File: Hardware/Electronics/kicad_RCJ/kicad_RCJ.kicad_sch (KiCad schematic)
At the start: 66 parts, among them J1 Raspberry_Pi_2_3, J2 Conn_01x06, J3 Conn_01x02, J4 Conn_01x02, J5 Conn_01x02, J6 Conn_01x02, J7 Conn_01x01, U20 BNO085, U21 ICM20948, U22 LSM6DSOX+LIS3MDL, U23 TCS34725, U24 APDS9960

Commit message: schematic finished?
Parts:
- removed D1, D2: ~, symbol RCJ_parts:small_LED
- removed F1: Fuse, symbol Device:Fuse
- added J10, J11, J12, J13, J15: Conn_01x04, symbol Connector_Generic:Conn_01x04
- added J14: Conn_01x06_teensy_left, symbol Connector_Generic:Conn_01x06
- added J16: Conn_01x07, symbol Connector_Generic:Conn_01x07
- added J8: Conn_01x03, symbol Connector_Generic:Conn_01x03
- added J9: Conn_01x06_LED, symbol Connector_Generic:Conn_01x06
- added U25: ~, symbol RCJ_parts:VL53L0X/VL53L1X
- J4: value Conn_01x02 -> Conn_01x02_5V
- J5: value Conn_01x02 -> Conn_01x02_3V3
- J6: value Conn_01x02 -> Conn_01x02_I2C
- J7: value Conn_01x01 -> Conn_01x01_LOP
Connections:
- net +3.3V: now also U25.2 (VIN)
- net +5V: now also D3.2 (VIN), D4.2 (VIN), D5.2 (VIN), D6.2 (VIN), D7.1 (VIN), D8.1 (VIN); no longer J1.2 (5V)
- net GND: now also U6.44 (GND), U25.3 (GND); no longer J1.6 (GND)
- net SCL: now also U25.5 (SCL)
- net SCL1: no longer J1.5 (SCL/GPIO3)
- net SDA: now also U25.4 (SDA)
- net SDA1: no longer J1.3 (SDA/GPIO2)
- net at R14.1, U10.1 (VIN), U11.1 (VIN)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: now also BT1.1 (+)
- net at U19.1 (PA0): now also J16.7 (Pin_7)
- net at U19.16 (PB7): now also U25.6 (XSHUT)
- net at U19.19 (IB): now also J8.3 (Pin_3)
- net at U19.2 (PA1): now also J16.6 (Pin_6)
- net at U19.20 (RST): now also J8.2 (Pin_2)
- net at U19.21 (IA): now also J8.1 (Pin_1)
- net at U19.3 (PA2): now also J16.5 (Pin_5)
- net at U19.4 (PA3): now also J16.4 (Pin_4)
- net at U19.5 (PA4): now also J16.3 (Pin_3)
- net at U19.6 (PA5): now also J16.2 (Pin_2)
- net at U19.7 (PA6): now also J16.1 (Pin_1)
- net at D8.2 (SIGNAL): now also J9.1 (Pin_1); no longer D7.2 (SIGNAL)
- net at D5.3 (SIGNAL): now also J9.5 (Pin_5)
- net at U1.12 (IMODE): now also J10.1 (Pin_1)
- net at U1.13 (FAULT): now also J10.2 (Pin_2)
- net at U1.14 (CS): now also J10.3 (Pin_3)
- net at U1.7 (VREF): now also J10.4 (Pin_4)
- net at D3.3 (SIGNAL): now also J9.4 (Pin_4)
- net at D6.3 (SIGNAL): now also J9.6 (Pin_6)
- net at U2.12 (IMODE): now also J11.1 (Pin_1)
- net at U2.13 (FAULT): now also J11.2 (Pin_2)
- net at U2.14 (CS): now also J11.3 (Pin_3)
- net at U2.7 (VREF): now also J11.4 (Pin_4)
- net at U4.12 (IMODE): now also J13.1 (Pin_1)
- net at U4.13 (FAULT): now also J13.2 (Pin_2)
- net at U4.14 (CS): now also J13.3 (Pin_3)
- net at U4.7 (VREF): now also J13.4 (Pin_4)
- net at U3.12 (IMODE): now also J12.1 (Pin_1)
- net at U3.13 (FAULT): now also J12.2 (Pin_2)
- net at U3.14 (CS): now also J12.3 (Pin_3)
- net at U3.7 (VREF): now also J12.4 (Pin_4)
- net at D4.3 (SIGNAL): now also J9.3 (Pin_3)
- net at U6.12 (12/MISO): now also J14.6 (Pin_6)
- net at U6.21 (21/A7/RX5): now also J15.1 (Pin_1)
- net at U6.24 (24/A10/TX6/SCL2): now also J14.5 (Pin_5)
- net at U6.25 (25/A11/RX6/SDA2): now also J14.4 (Pin_4)
- net at U6.26 (26/A12/MOSI1): now also J14.3 (Pin_3)
- net at U6.27 (27/A13/SCK1): now also J14.2 (Pin_2)
- net at U6.32: now also J14.1 (Pin_1)
- net at U6.37 (37/CS): now also J15.4 (Pin_4)
- net at U6.38 (38/A14/(CS1)): now also J15.3 (Pin_3)
- net at U6.39 (39/A15/(MISO1)): now also J15.2 (Pin_2)
- new net: D7.2 (SIGNAL), J9.2 (Pin_2)
- no-connect marks 57 -> 89
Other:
- note added: "ENCODER LOGIC LEVELS MUST BE FIXED? I tested it and it should work?"
- note removed: "ENCODER LOGIC LEVELS MUST BE FIXED"
- moved on the sheet: J2, J3, J4, J5, R1, R10, R11, R12, R2, R3, R4, R5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

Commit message: assigned some footprints
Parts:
- J10: value Conn_01x04 -> Conn_01x04_M1_extra; footprint (none) -> Connector_PinSocket_2.54mm:PinSocket_1x04_P2.54mm_Vertical
- J11: value Conn_01x04 -> Conn_01x04_M2_extra; footprint (none) -> Connector_PinSocket_2.54mm:PinSocket_1x04_P2.54mm_Vertical
- J12: value Conn_01x04 -> Conn_01x04_M3_extra; footprint (none) -> Connector_PinSocket_2.54mm:PinSocket_1x04_P2.54mm_Vertical
- J13: value Conn_01x04 -> Conn_01x04_M4_extra; footprint (none) -> Connector_PinSocket_2.54mm:PinSocket_1x04_P2.54mm_Vertical
- J14: value Conn_01x06_teensy_left -> Conn_01x06_teensy_left_extra; footprint (none) -> Connector_PinSocket_2.54mm:PinSocket_1x06_P2.54mm_Vertical
- J15: value Conn_01x04 -> Conn_01x04_teensy_right_extra; footprint (none) -> Connector_PinSocket_2.54mm:PinSocket_1x04_P2.54mm_Vertical
- J16: value Conn_01x07 -> Conn_01x07_IO_expander_extra; footprint (none) -> Connector_PinSocket_2.54mm:PinSocket_1x07_P2.54mm_Vertical
- J2: value Conn_01x06 -> Conn_01x06_IMU_extra; footprint (none) -> Connector_PinSocket_2.54mm:PinSocket_1x06_P2.54mm_Vertical
- J3: value Conn_01x02 -> Conn_01x02_colsens_interrupt; footprint (none) -> Connector_PinSocket_2.54mm:PinSocket_1x02_P2.54mm_Vertical
- J4, J5: footprint (none) -> Connector_JST:JST_XH_B2B-XH-A_1x02_P2.50mm_Vertical
- J6: value Conn_01x02_I2C -> Conn_01x02_I2C1; footprint (none) -> Connector_JST:JST_XH_B2B-XH-A_1x02_P2.50mm_Vertical
- J7, J9: footprint (none) -> Connector_PinSocket_2.54mm:PinSocket_1x01_P2.54mm_Vertical
- J8: value Conn_01x03 -> Conn_01x03_IO_expander_interrupts_extra; footprint (none) -> Connector_JST:JST_XH_B3B-XH-A_1x03_P2.50mm_Vertical
- M1, M2, M3, M4: footprint (none) -> Connector_PinHeader_2.54mm:PinHeader_1x06_P2.54mm_Vertical
- M5, M6: footprint (none) -> Connector_PinHeader_2.54mm:PinHeader_1x03_P2.54mm_Vertical
- S5: footprint (none) -> Connector_JST:JST_XH_B3B-XH-A_1x03_P2.50mm_Vertical
- U12, U13, U14, U15, U16, U17, U18, U25: footprint (none) -> Connector_JST:JST_XH_B6B-XH-A_1x06_P2.50mm_Vertical

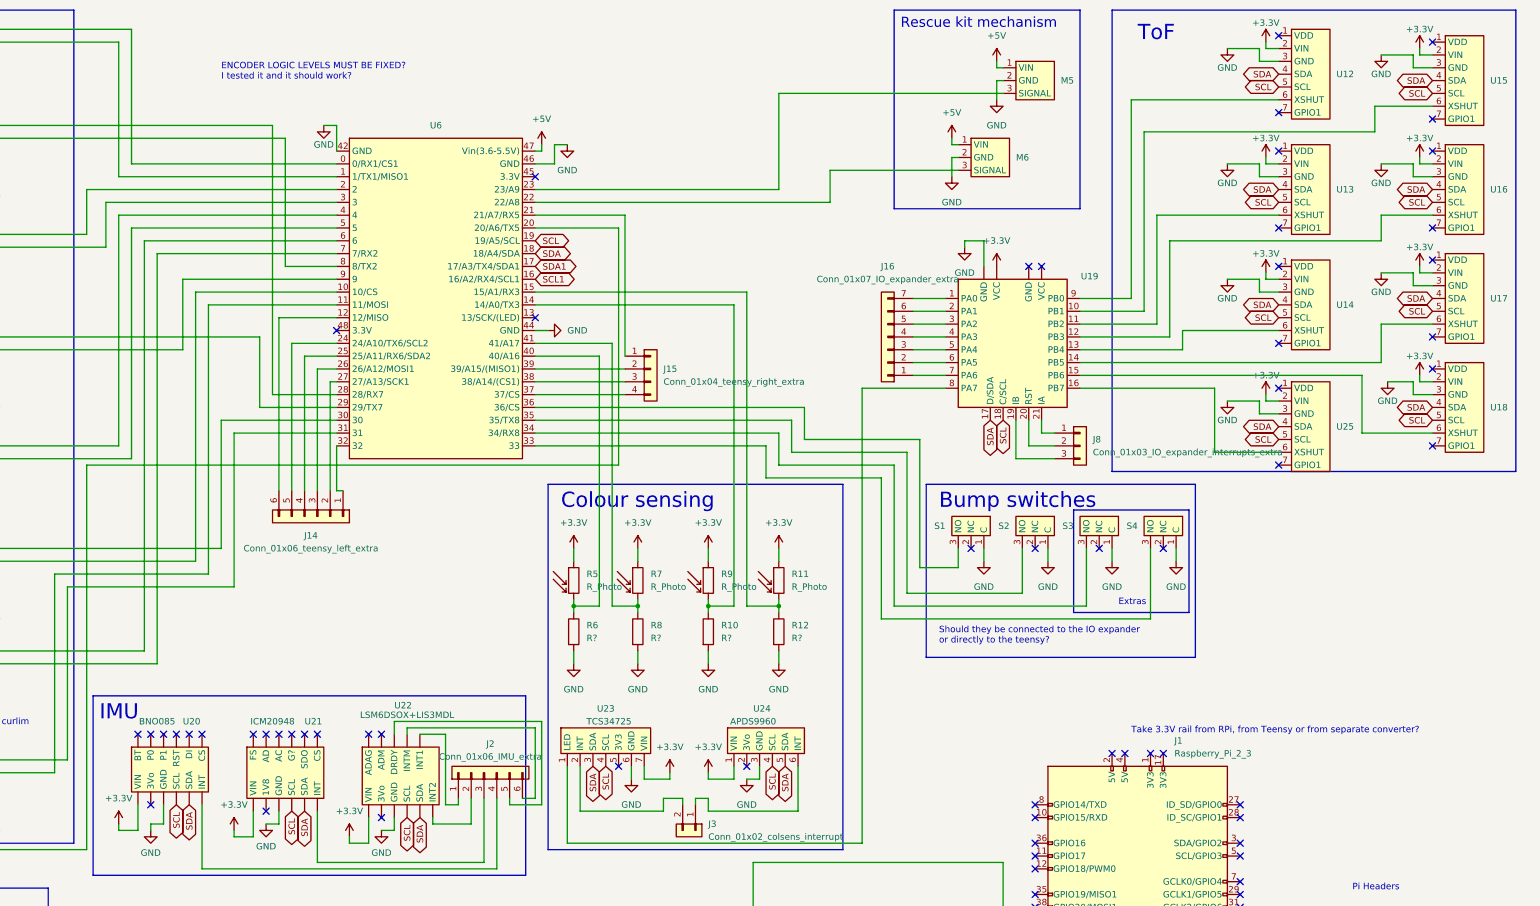
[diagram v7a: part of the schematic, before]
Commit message: clarified schematic and added some headers
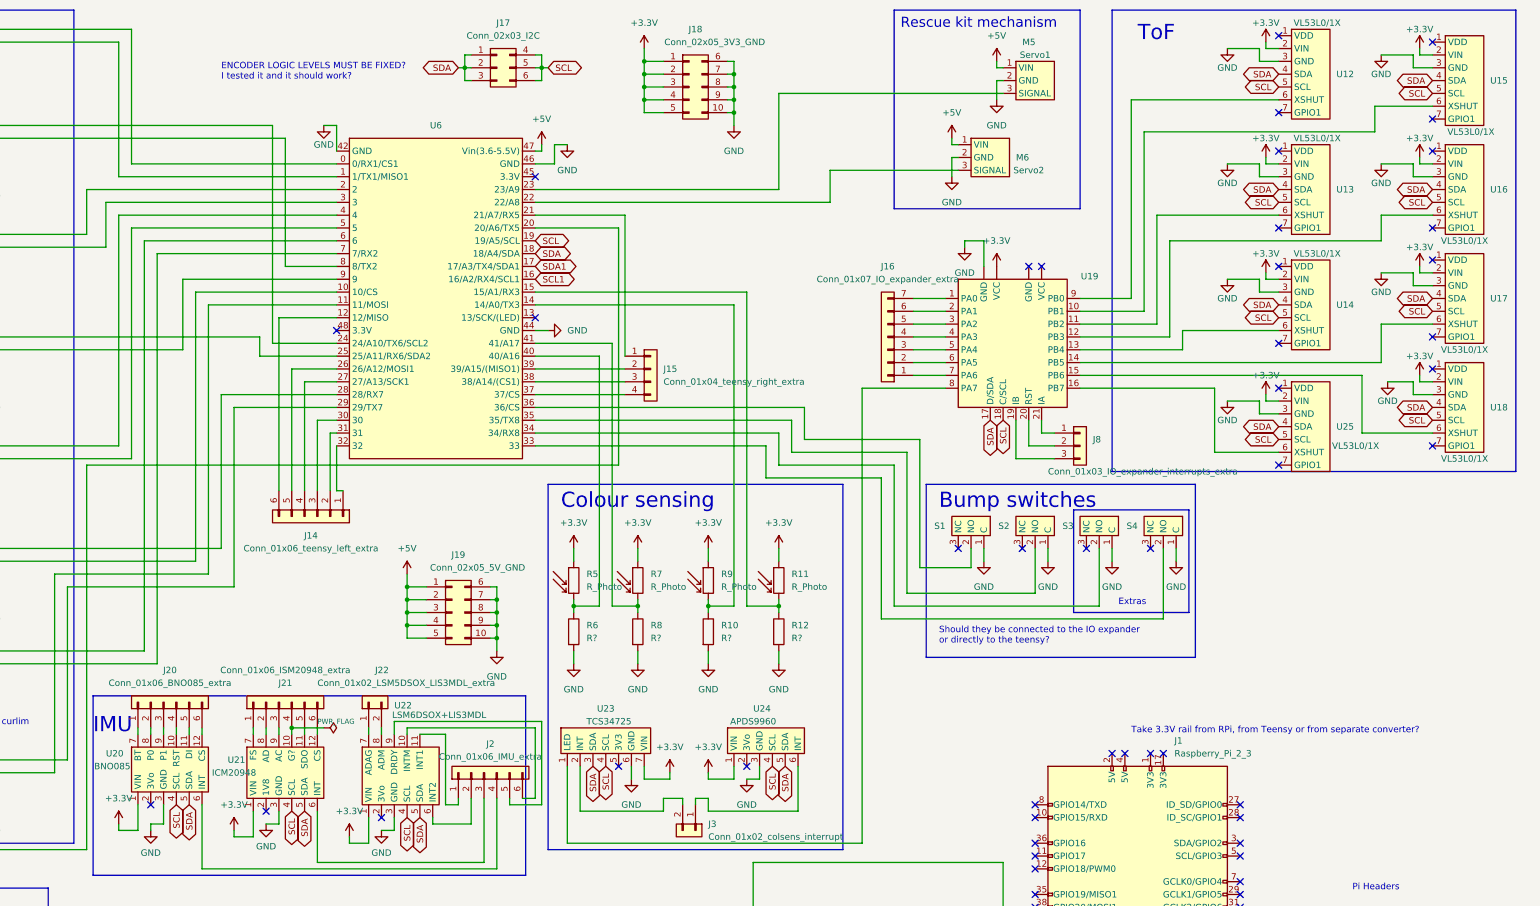
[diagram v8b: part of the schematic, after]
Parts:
- added J17: Conn_02x03_I2C, symbol Connector_Generic:Conn_02x03_Top_Bottom
- added J18: Conn_02x05_3V3_GND, symbol Connector_Generic:Conn_02x05_Top_Bottom
- added J19: Conn_02x05_5V_GND, symbol Connector_Generic:Conn_02x05_Top_Bottom
- added J20: Conn_01x06_BNO085_extra, symbol Connector_Generic:Conn_01x06
- added J21: Conn_01x06_ISM20948_extra, symbol Connector_Generic:Conn_01x06
- added J22: Conn_01x02_LSM5DSOX_LIS3MDL_extra, symbol Connector_Generic:Conn_01x02
- M5: value ~ -> Servo1
- M6: value ~ -> Servo2
- U12, U13, U14, U15, U16, U17, U18, U25: value ~ -> VL53L0/1X
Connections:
- net +3.3V: now also U20.1 (VIN), U21.1 (VIN), U22.1 (VIN), J18.1 (Pin_1), J18.2 (Pin_2), J18.3 (Pin_3), J18.4 (Pin_4), J18.5 (Pin_5); no longer U20. (VIN), U21. (VIN), U22. (VIN)
- net +5V: now also J19.1 (Pin_1), J19.2 (Pin_2), J19.3 (Pin_3), J19.4 (Pin_4), J19.5 (Pin_5)
- net GND: now also U20.3 (GND), U21.3 (GND), U22.3 (GND), J18.10 (Pin_10), J18.6 (Pin_6), J18.7 (Pin_7), J18.8 (Pin_8), J18.9 (Pin_9), J19.10 (Pin_10), J19.6 (Pin_6), J19.7 (Pin_7), J19.8 (Pin_8), J19.9 (Pin_9); no longer U20. (VIN), U21. (VIN), U22. (VIN)
- net SCL: now also U20.4 (SCL), U21.4 (SCL), U22.4 (SCL), J17.4 (Pin_4), J17.5 (Pin_5), J17.6 (Pin_6); no longer U20. (VIN), U21. (VIN), U22. (VIN)
- net SDA: now also U20.5 (SDA), U21.5 (SDA), U22.5 (SDA), J17.1 (Pin_1), J17.2 (Pin_2), J17.3 (Pin_3); no longer U20. (VIN), U21. (VIN), U22. (VIN)
- net at J2.3 (Pin_3): now also U21.6 (INT); no longer U21. (VIN)
- net at S3.2 (NO): now also U6.34 (34/RX8)
- net at S3.3 (NC): no longer U6.34 (34/RX8)
- net at S1.2 (NO): now also U6.36 (36/CS)
- net at S1.3 (NC): no longer U6.36 (36/CS)
- net at U1.4 (PH/IN2): now also U6.24 (24/A10/TX6/SCL2); no longer U6.28 (28/RX7)
- net at J14.2 (Pin_2): now also U6.31; no longer U6.27 (27/A13/SCK1)
- net at J14.3 (Pin_3): now also U6.30; no longer U6.26 (26/A12/MOSI1)
- net at J14.4 (Pin_4): now also U6.27 (27/A13/SCK1); no longer U6.25 (25/A11/RX6/SDA2)
- net at J14.5 (Pin_5): now also U6.26 (26/A12/MOSI1); no longer U6.24 (24/A10/TX6/SCL2)
- net at S4.2 (NO): now also U6.33
- net at S4.3 (NC): no longer U6.33
- net at J2.1 (Pin_1): now also U22.11 (INT1); no longer U22. (VIN)
- net at J2.2 (Pin_2): now also U22.6 (INT2); no longer U22. (VIN)
- net at J2.5 (Pin_5): now also U22.9 (DRDY); no longer U22. (VIN)
- net at J2.6 (Pin_6): now also U22.10 (INTM); no longer U22. (VIN)
- net at U2.4 (PH/IN2): now also U6.25 (25/A11/RX6/SDA2); no longer U6.29 (29/TX7)
- net at J2.4 (Pin_4): now also U20.6 (INT); no longer U20. (VIN)
- net at U4.4 (PH/IN2): now also U6.29 (29/TX7); no longer U6.31
- net at U3.4 (PH/IN2): now also U6.28 (28/RX7); no longer U6.30
- net at U6.35 (35/TX8): now also S2.2 (NO); no longer S2.3 (NO)
- new net: J21.4 (Pin_4), U21.10 (G?)
- new net: J21.5 (Pin_5), U21.11 (SDO)
- new net: J21.6 (Pin_6), U21.12 (CS)
- new net: J21.1 (Pin_1), U21.7 (FS)
- new net: J21.2 (Pin_2), U21.8 (AD)
- new net: J21.3 (Pin_3), U21.9 (AC)
- new net: J22.1 (Pin_1), U22.7 (ADAG)
- new net: J22.2 (Pin_2), U22.8 (ADM)
- new net: J20.1 (Pin_1), U20.7 (BT)
- new net: J20.2 (Pin_2), U20.8 (P0)
- new net: J20.3 (Pin_3), U20.9 (P1)
- new net: J20.4 (Pin_4), U20.10 (RST)
- new net: J20.5 (Pin_5), U20.11 (DI)
- new net: J20.6 (Pin_6), U20.12 (CS)
- no-connect marks 89 -> 75
